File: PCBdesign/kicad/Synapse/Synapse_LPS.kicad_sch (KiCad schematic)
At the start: 12 parts, among them J1 SSW-102-01-G-S, J2 SSW-102-01-G-S, P1 TSW-102-07-G-S, P2 TSW-102-07-G-S, P3 TSW-102-07-G-S

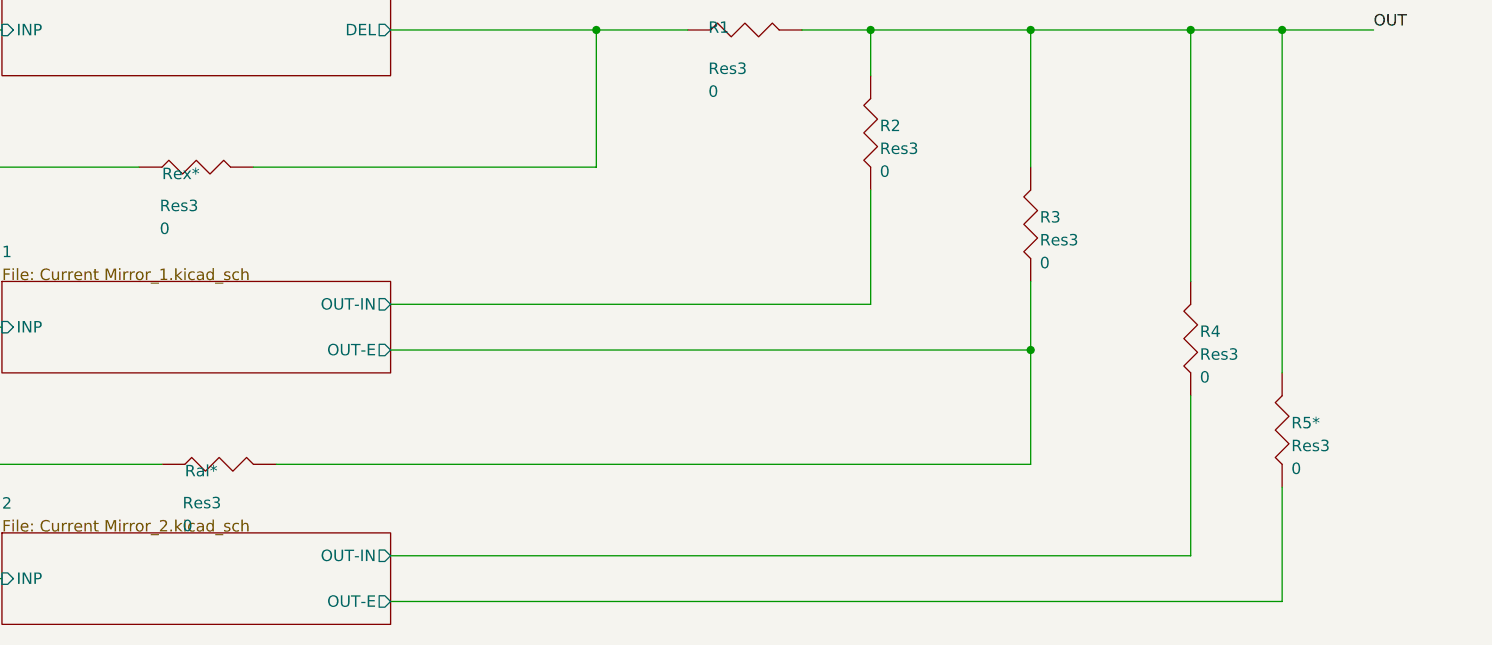
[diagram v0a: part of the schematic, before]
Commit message: Add annotation script, wiring checklist for breadboarding, and .gitignore in case proprietary libs are added. Fix annotations that were missing after KiCad import in the schematics.
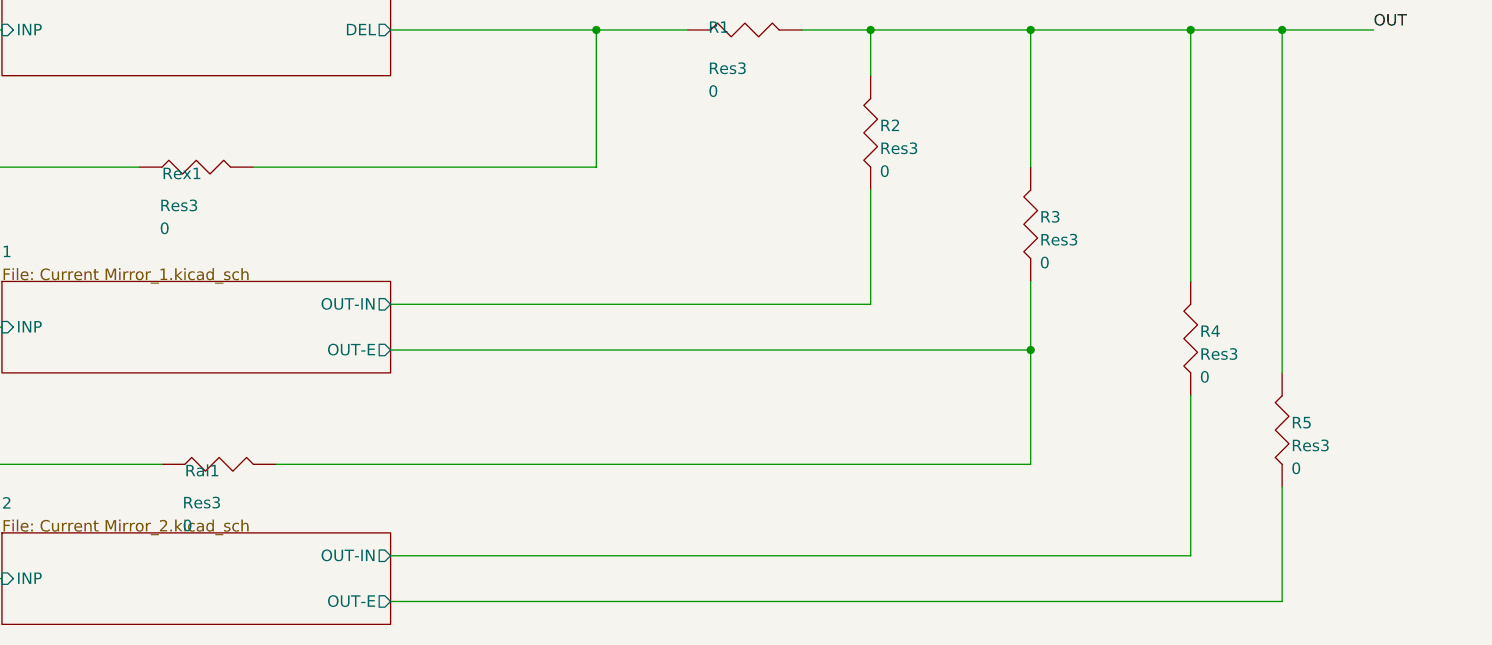
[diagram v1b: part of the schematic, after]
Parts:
- renumbered R5* to R5, Ral* to Ral1, Rex* to Rex1
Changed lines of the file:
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@@
 		(in_pos_files yes)
 		(dnp no)
-		(property "Reference" "#PWR?"
+		(property "Reference" "#PWR027"
 			(at 154.94 60.1472 0)
 			(hide yes)
@@
 			(project "Synapse_LPS"
 				(path "/af4a7426-c915-4fd8-a9a0-d1d0653890c7"
-					(reference "#PWR?")
+					(reference "#PWR027")
 					(unit 1)
 				)
@@
 		(in_pos_files yes)
 		(dnp no)
-		(property "Reference" "R5*"
+		(property "Reference" "R5"
 			(at 211.836 131.0132 0)
 			(show_name no)
@@
 			(project "Synapse_LPS"
 				(path "/af4a7426-c915-4fd8-a9a0-d1d0653890c7"
-					(reference "R5*")
+					(reference "R5")
 					(unit 1)
 				)
@@
 		(in_pos_files yes)
 		(dnp no)
-		(property "Reference" "#PWR?"
+		(property "Reference" "#PWR028"
 			(at 157.48 52.5272 0)
 			(hide yes)
@@
 			(project "Synapse_LPS"
 				(path "/af4a7426-c915-4fd8-a9a0-d1d0653890c7"
-					(reference "#PWR?")
+					(reference "#PWR028")
 					(unit 1)
 				)
@@
 		(in_pos_files yes)
 		(dnp no)
-		(property "Reference" "#PWR?"
+		(property "Reference" "#PWR025"
 			(at 121.92 52.5272 0)
 			(hide yes)
@@
 			(project "Synapse_LPS"
 				(path "/af4a7426-c915-4fd8-a9a0-d1d0653890c7"
-					(reference "#PWR?")
+					(reference "#PWR025")
 					(unit 1)
 				)
@@
 		(in_pos_files yes)
 		(dnp no)
-		(property "Reference" "Ral*"
+		(property "Reference" "Ral1"
 			(at 88.9 136.3472 90)
 			(show_name no)
@@
 			(project "Synapse_LPS"
 				(path "/af4a7426-c915-4fd8-a9a0-d1d0653890c7"
-					(reference "Ral*")
+					(reference "Ral1")
 					(unit 1)
 				)
@@
 		(in_pos_files yes)
 		(dnp no)
-		(property "Reference" "#PWR?"
+		(property "Reference" "#PWR024"
 			(at 119.38 60.1472 0)
 			(hide yes)
@@
 			(project "Synapse_LPS"
 				(path "/af4a7426-c915-4fd8-a9a0-d1d0653890c7"
-					(reference "#PWR?")
+					(reference "#PWR024")
 					(unit 1)
 				)
@@
 		(in_pos_files yes)
 		(dnp no)
-		(property "Reference" "#PWR?"
+		(property "Reference" "#PWR030"
 			(at 175.26 52.5272 0)
 			(hide yes)
@@
 			(project "Synapse_LPS"
 				(path "/af4a7426-c915-4fd8-a9a0-d1d0653890c7"
-					(reference "#PWR?")
+					(reference "#PWR030")
 					(unit 1)
 				)
@@
 		(in_pos_files yes)
 		(dnp no)
-		(property "Reference" "#PWR?"
+		(property "Reference" "#PWR023"
 			(at 101.6 60.1472 0)
 			(hide yes)
@@
 			(project "Synapse_LPS"
 				(path "/af4a7426-c915-4fd8-a9a0-d1d0653890c7"
-					(reference "#PWR?")
+					(reference "#PWR023")
 					(unit 1)
 				)
@@
 		(in_pos_files yes)
 		(dnp no)
-		(property "Reference" "#PWR?"
+		(property "Reference" "#PWR029"
 			(at 172.72 60.1472 0)
 			(hide yes)
@@
 			(project "Synapse_LPS"
 				(path "/af4a7426-c915-4fd8-a9a0-d1d0653890c7"
-					(reference "#PWR?")
+					(reference "#PWR029")
 					(unit 1)
 				)
@@
 		(in_pos_files yes)
 		(dnp no)
-		(property "Reference" "#PWR?"
+		(property "Reference" "#PWR026"
 			(at 137.16 60.1472 0)
 			(hide yes)
@@
 			(project "Synapse_LPS"
 				(path "/af4a7426-c915-4fd8-a9a0-d1d0653890c7"
-					(reference "#PWR?")
+					(reference "#PWR026")
 					(unit 1)
 				)
@@
 		(in_pos_files yes)
 		(dnp no)
-		(property "Reference" "Rex*"
+		(property "Reference" "Rex1"
 			(at 86.36 103.3272 90)
 			(show_name no)
@@
 			(project "Synapse_LPS"
 				(path "/af4a7426-c915-4fd8-a9a0-d1d0653890c7"
-					(reference "Rex*")
+					(reference "Rex1")
 					(unit 1)
 				)
